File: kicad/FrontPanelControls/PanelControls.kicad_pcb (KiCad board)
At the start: 2 copper layers, 106 x 37.8 mm, 48 parts, among them J1 BUTTON_A, J2 BUTTON_B, J3 BUTTON_C, J4 BUTTON_D, J5 Conn_02x04_Odd_Even, SW1 ADJ, U1 ADS1115IDGS, U2 TCA9534, U3 WS2812D, U4 WS2812D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

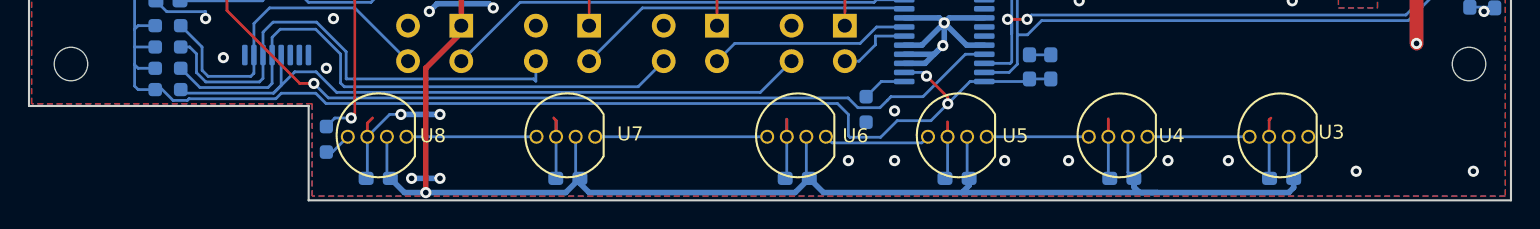
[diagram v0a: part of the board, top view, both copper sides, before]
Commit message: Move to fit new 3.5mm holes
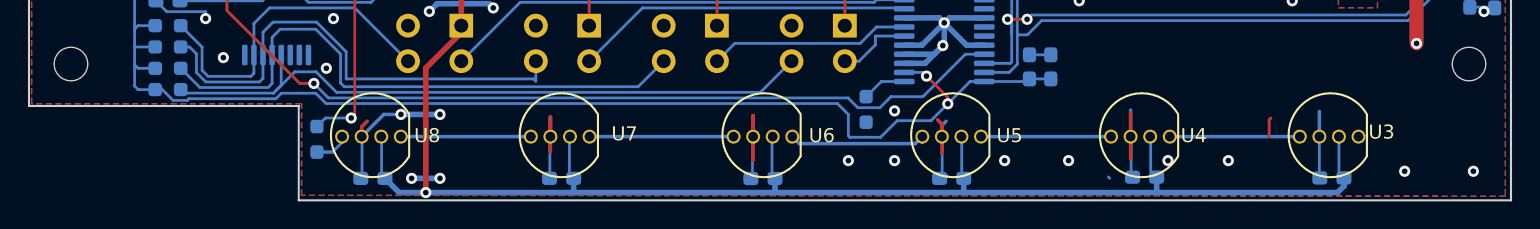
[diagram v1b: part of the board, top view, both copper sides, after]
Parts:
- moved C5 3.59 mm to (184.2, 154.1)
- moved U3 3.59 mm to (185.1, 148.0)
- moved C8 2.46 mm to (143.5, 154.2)
- moved U6 2.41 mm to (144.6, 148.0)
- moved C6 1.63 mm to (170.8, 154.1)
- moved U4 1.59 mm to (171.6, 148.0)
- moved R1 0.67 mm to (111.6, 151.4)
- moved C9 0.45 mm to (129.1, 154.2)
- moved U5 0.41 mm to (158.1, 148.0)
- moved U7 0.41 mm to (130.1, 148.0)
- moved U8 0.41 mm to (116.6, 148.0)
- moved C7 0.39 mm to (157.0, 154.2)
- moved C10 0.38 mm to (115.6, 154.2)
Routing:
- net GND: track 78.4 -> 93.5 mm
- net Net-(U5-Pad4): track 7.66 -> 10.3 mm
- net Net-(U6-Pad4): track 12.3 -> 10.3 mm
- net Net-(U4-Pad4): track 7.30 -> 9.30 mm
- net Net-(U3-Pad4): track 7.30 -> 9.30 mm
- net +5v: track 151.3 -> 152.5 mm
- net Net-(R1-Pad2): track 1.99 -> 2.66 mm
- net LED_DATA: track 21.1 -> 21.8 mm
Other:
- outline, holes or cut-outs redrawn
- board text added: "ZC95-FrontPanel-Analog(back) v0.2-3.5mm"
- board text removed: "ZC95-FrontPanel-Analog(back) v0.2"
